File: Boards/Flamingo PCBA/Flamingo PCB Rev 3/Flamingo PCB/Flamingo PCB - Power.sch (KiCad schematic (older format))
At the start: 23 parts, among them U501 3.3V_Reg, U502 1.8V_Reg

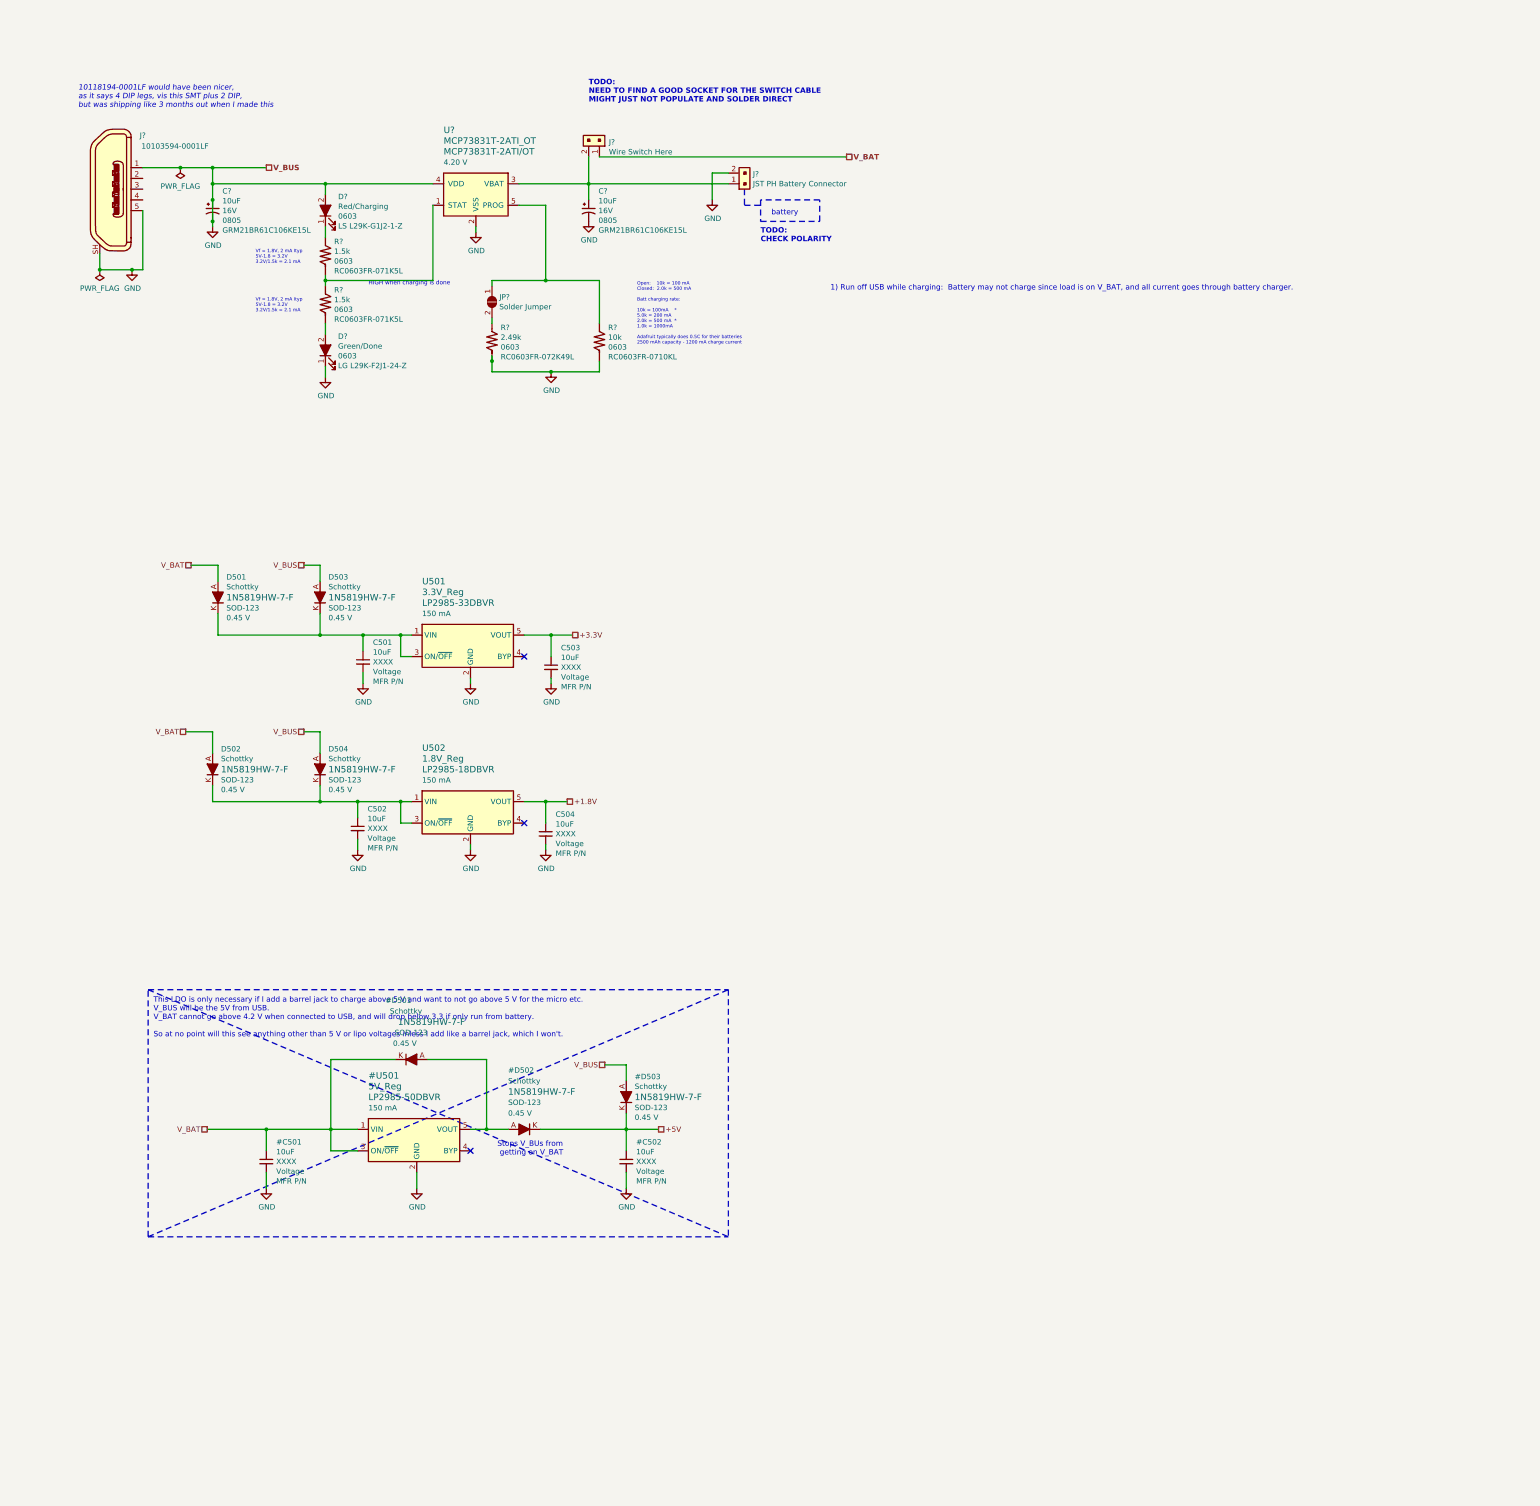
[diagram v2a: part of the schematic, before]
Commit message: Tidied up Power schematic, trying for load switching P-channel MOSFET
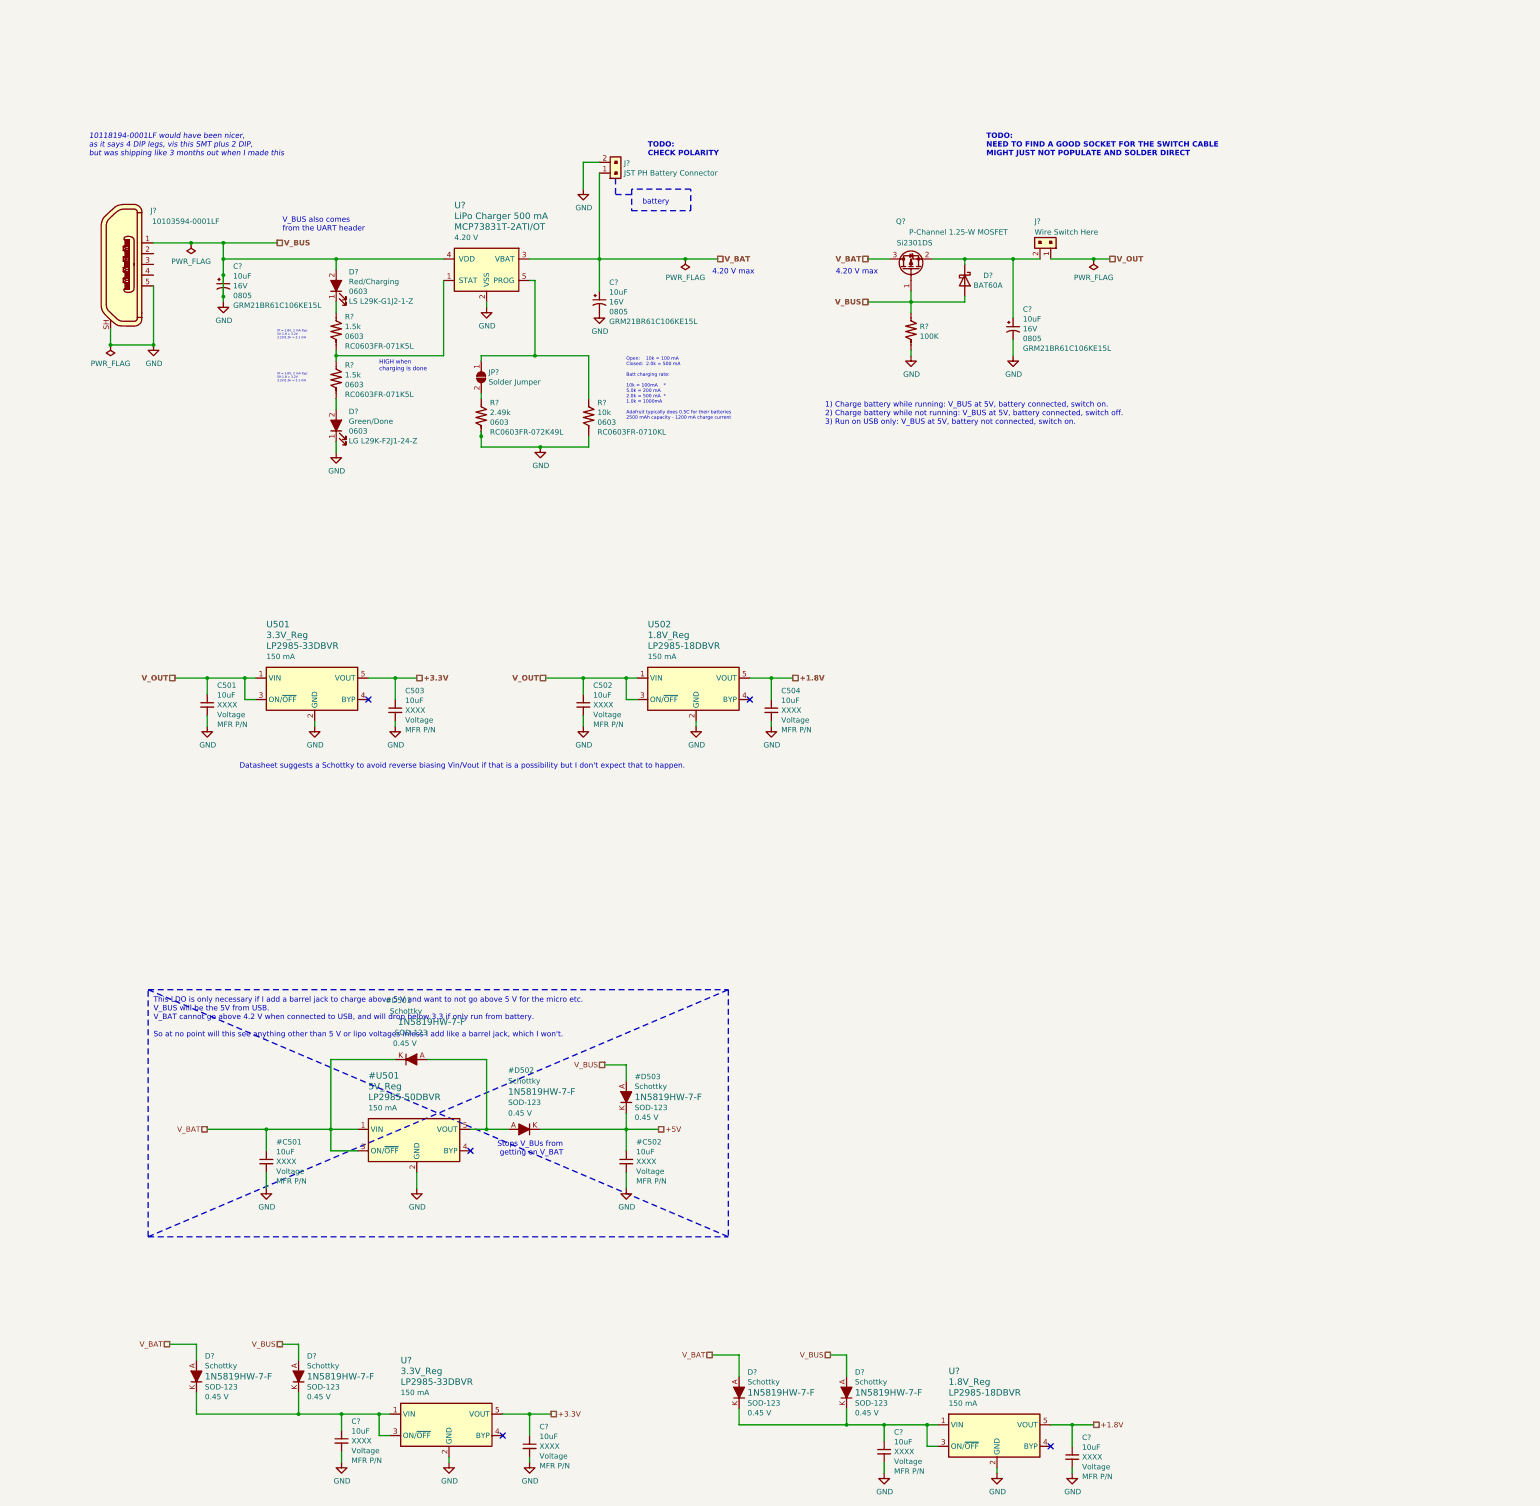
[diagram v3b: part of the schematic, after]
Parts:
- removed D501, D502, D503, D504: Schottky, digikey-footprints:SOD-123, symbol dk_Diodes-Rectifiers-Single:1N5819HW-7-F
- added C?: 10uF, Capacitors_SMD:C_0805_HandSoldering, symbol MyCapacitors:CP1_Small_vert
- added C? (x4): 10uF, symbol MyCapacitors:C_Small_vert
- added D?: BAT60A, Diode_SMD:D_SOD-323, symbol Diode:BAT60A
- added D? (x4): Schottky, digikey-footprints:SOD-123, symbol dk_Diodes-Rectifiers-Single:1N5819HW-7-F
- added Q?: P-Channel 1.25-W MOSFET, symbol Device:Q_PMOS_GSD
- added R?: 100K, symbol MyResistors:R_vert
- added U?: 3.3V_Reg, digikey-footprints:SOT-753, symbol MyICs:3.3V_Reg
- added U?: 1.8V_Reg, digikey-footprints:SOT-753, symbol MyICs:3.3V_Reg
- U?: value MCP73831T-2ATI_OT -> LiPo Charger 500 mA
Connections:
- net +1.8V: now also C?.1, U?.5 (VOUT)
- net +3.3V: now also C?.1, U?.5 (VOUT)
- net GND: now also C?.2, C?.2, C?.2, C?.2, C?.2, D?.2 (A), D?.A, D?.A, Q?.1 (G), R?.1, R?.2, U?.2 (GND), U?.2 (GND)
- net V_BAT: now also C?.1, J?.1, U?.3 (VBAT), D?.A, D?.A, Q?.3 (D); no longer J?.1
- net V_OUT: now reaches C501.1, U501.1 (VIN), U501.3 (ON/~OFF)
- net V_OUT: now also C502.1, J?.1, U502.1 (VIN), U502.3 (ON/~OFF)
- new net: C?.1, D?.1 (K), J?.2, Q?.2 (S)
- new net: C?.1, D?.K, D?.K, U?.1 (VIN), U?.3 (ON/~OFF) (x2)
- no-connect marks 3 -> 5
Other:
- note added: "1) Charge battery while running: V_BUS at 5V, battery connected, switch on.\n2) Charge battery while not running: V_BUS at 5V, battery connected, switch off.\n3) Run on USB only: V_BUS at 5V, battery not connected, switch on."
- note added: "4.20 V max"
- note added: "Datasheet suggests a Schottky to avoid reverse biasing Vin/Vout if that is a possibility but I don't expect that to happen."
- note added: "HIGH when\ncharging is done"
- note added: "V_BUS also comes\nfrom the UART header"
- note removed: "1) Run off USB while charging: Battery may not charge since load is on V_BAT, and all current goes through battery charger."
- note removed: "HIGH when charging is done"
- moved on the sheet: C501, C502, C503, C504, C?, D?, J?, JP?, R?, U501, U502, U?

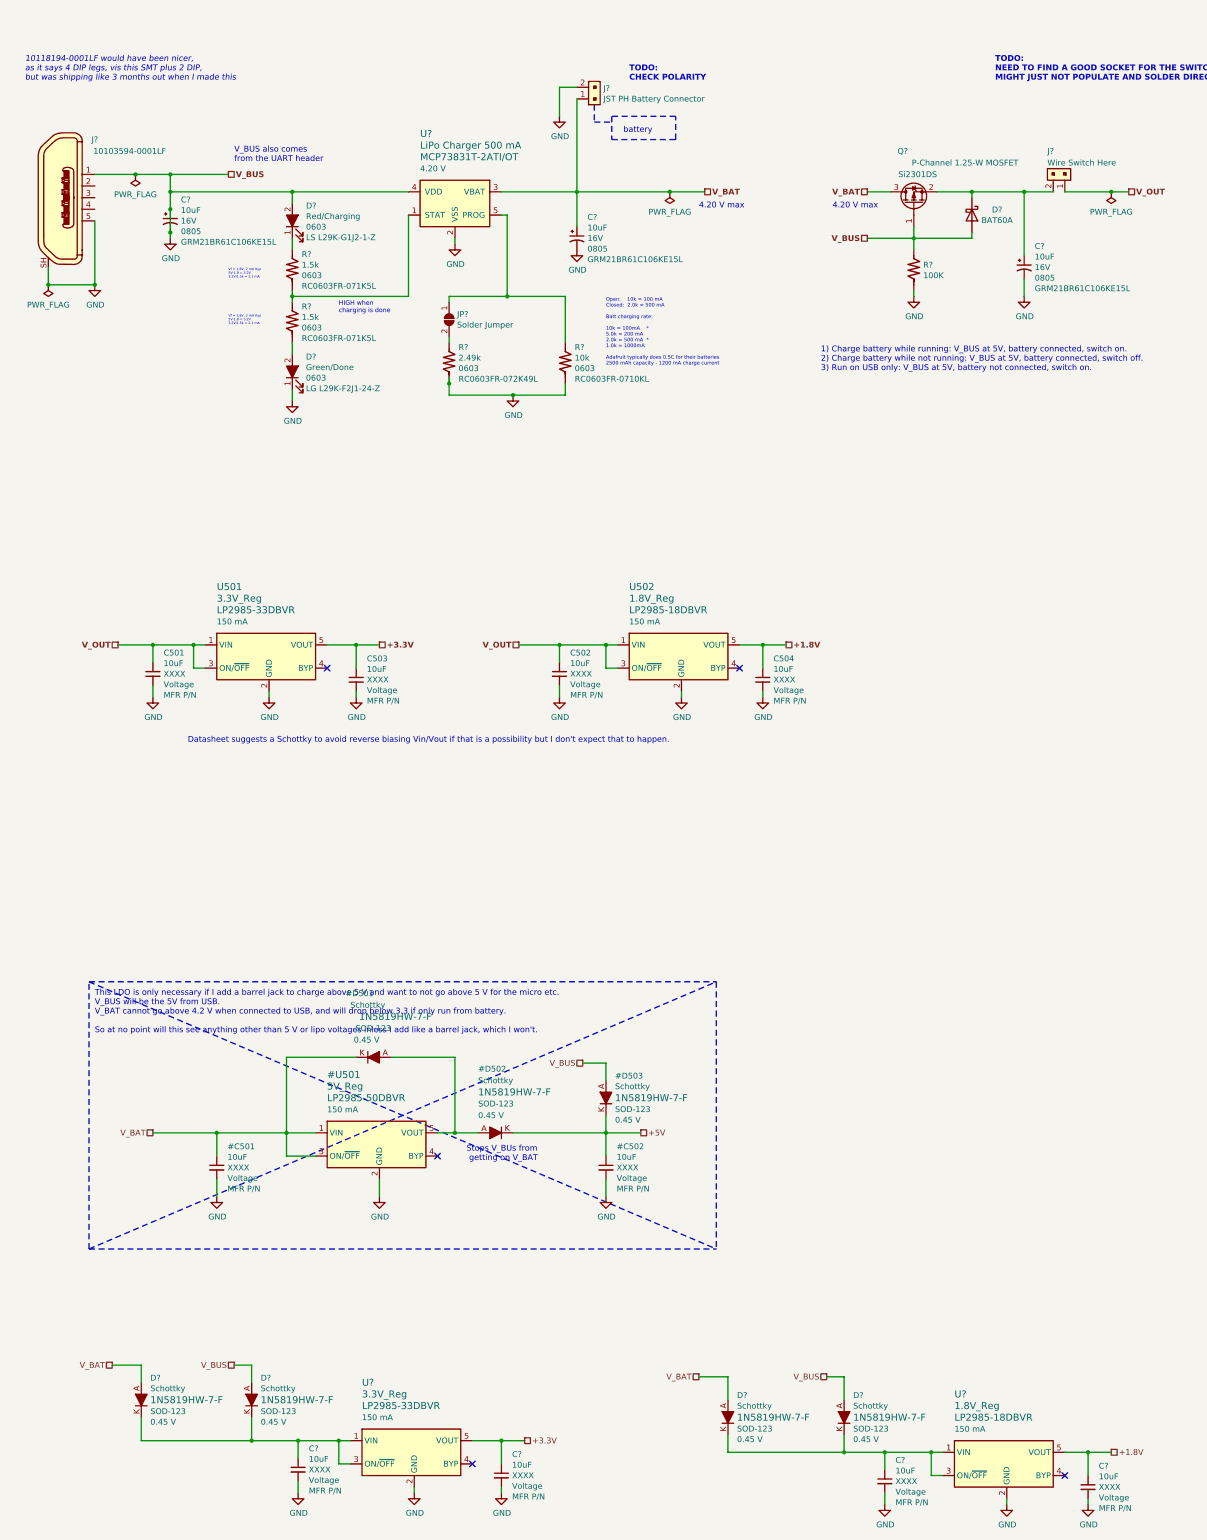
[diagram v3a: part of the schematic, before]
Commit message: More work on Arduino schematic, created button board schematic
Button board schematic should probably be a separate project
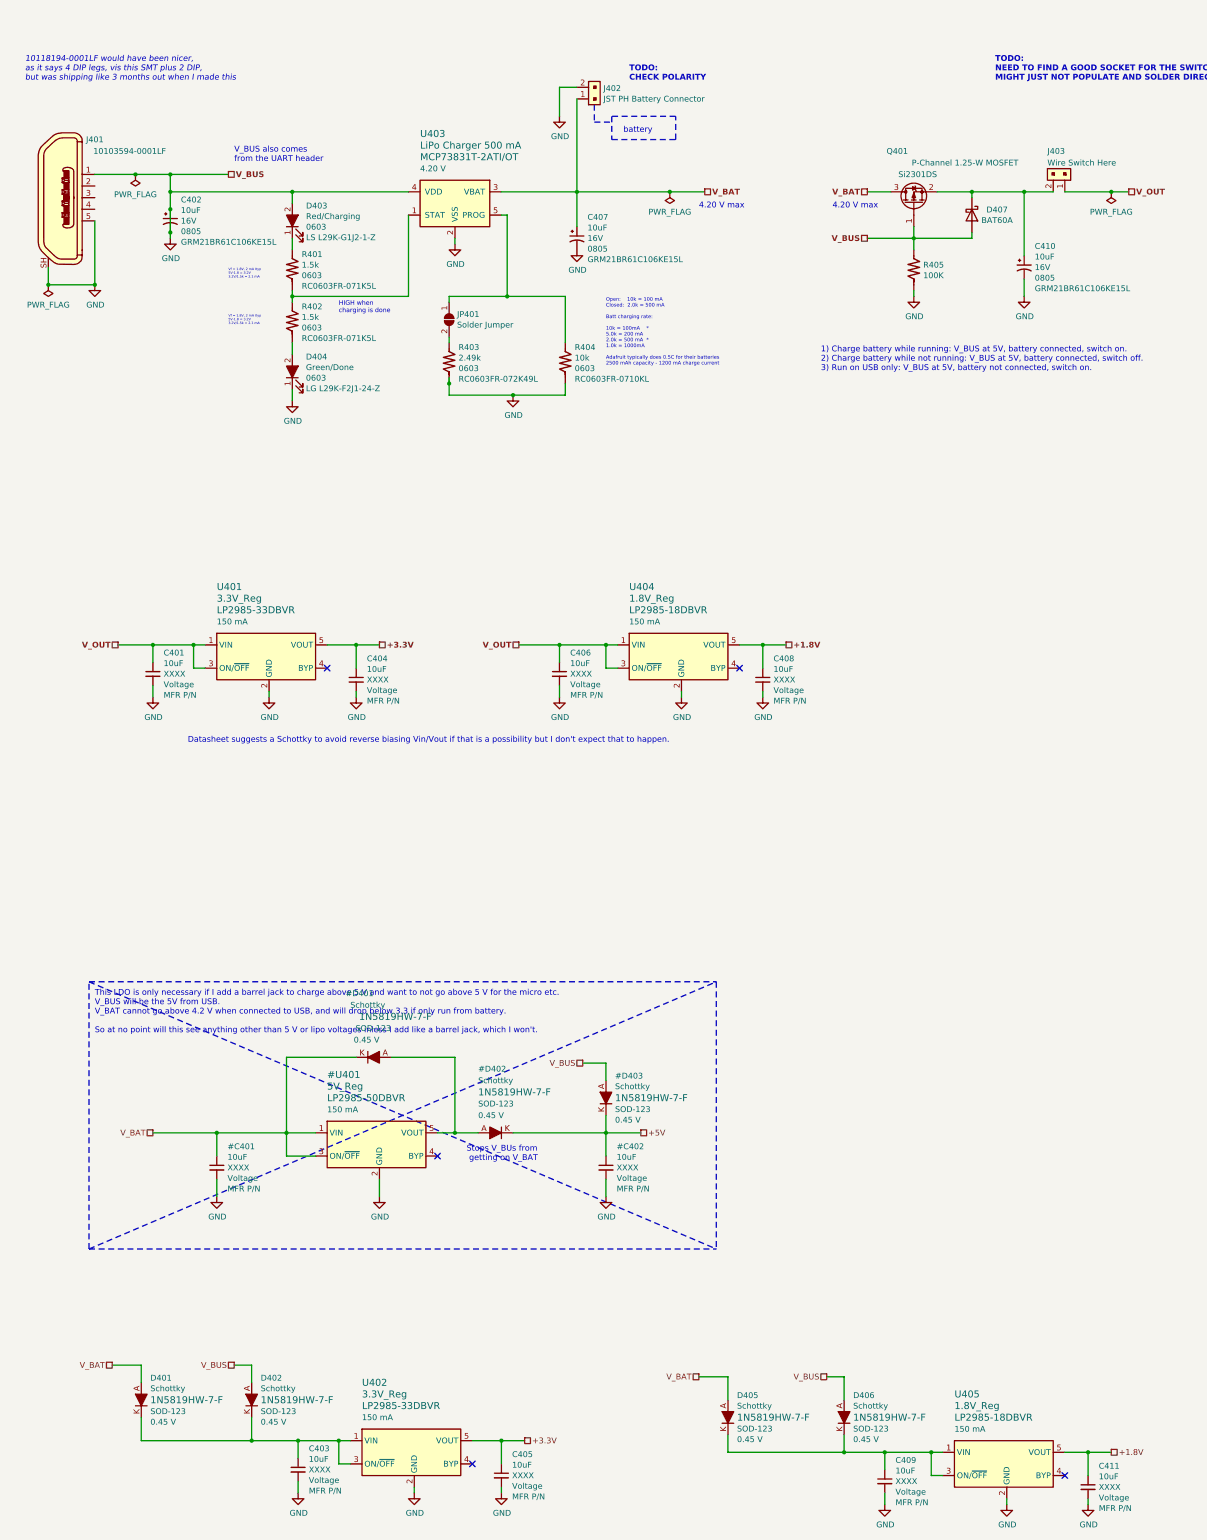
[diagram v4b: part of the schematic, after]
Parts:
- gave numbers to parts that had none: 27
- renumbered C501 to C401, C503 to C404, C502 to C406, C504 to C408, U501 to U401, U502 to U404
